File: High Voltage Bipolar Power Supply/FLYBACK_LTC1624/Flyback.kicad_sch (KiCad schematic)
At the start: 46 parts, among them J1 1715721, J2 Conn_01x02, Q1 PZT2222A, Q2 IRL540NS, T1 VP3-0138, U1 LTC1624CS8, U2 TSR_1-2450, U3 ADUM4195-1, U4 TBA1-0511E

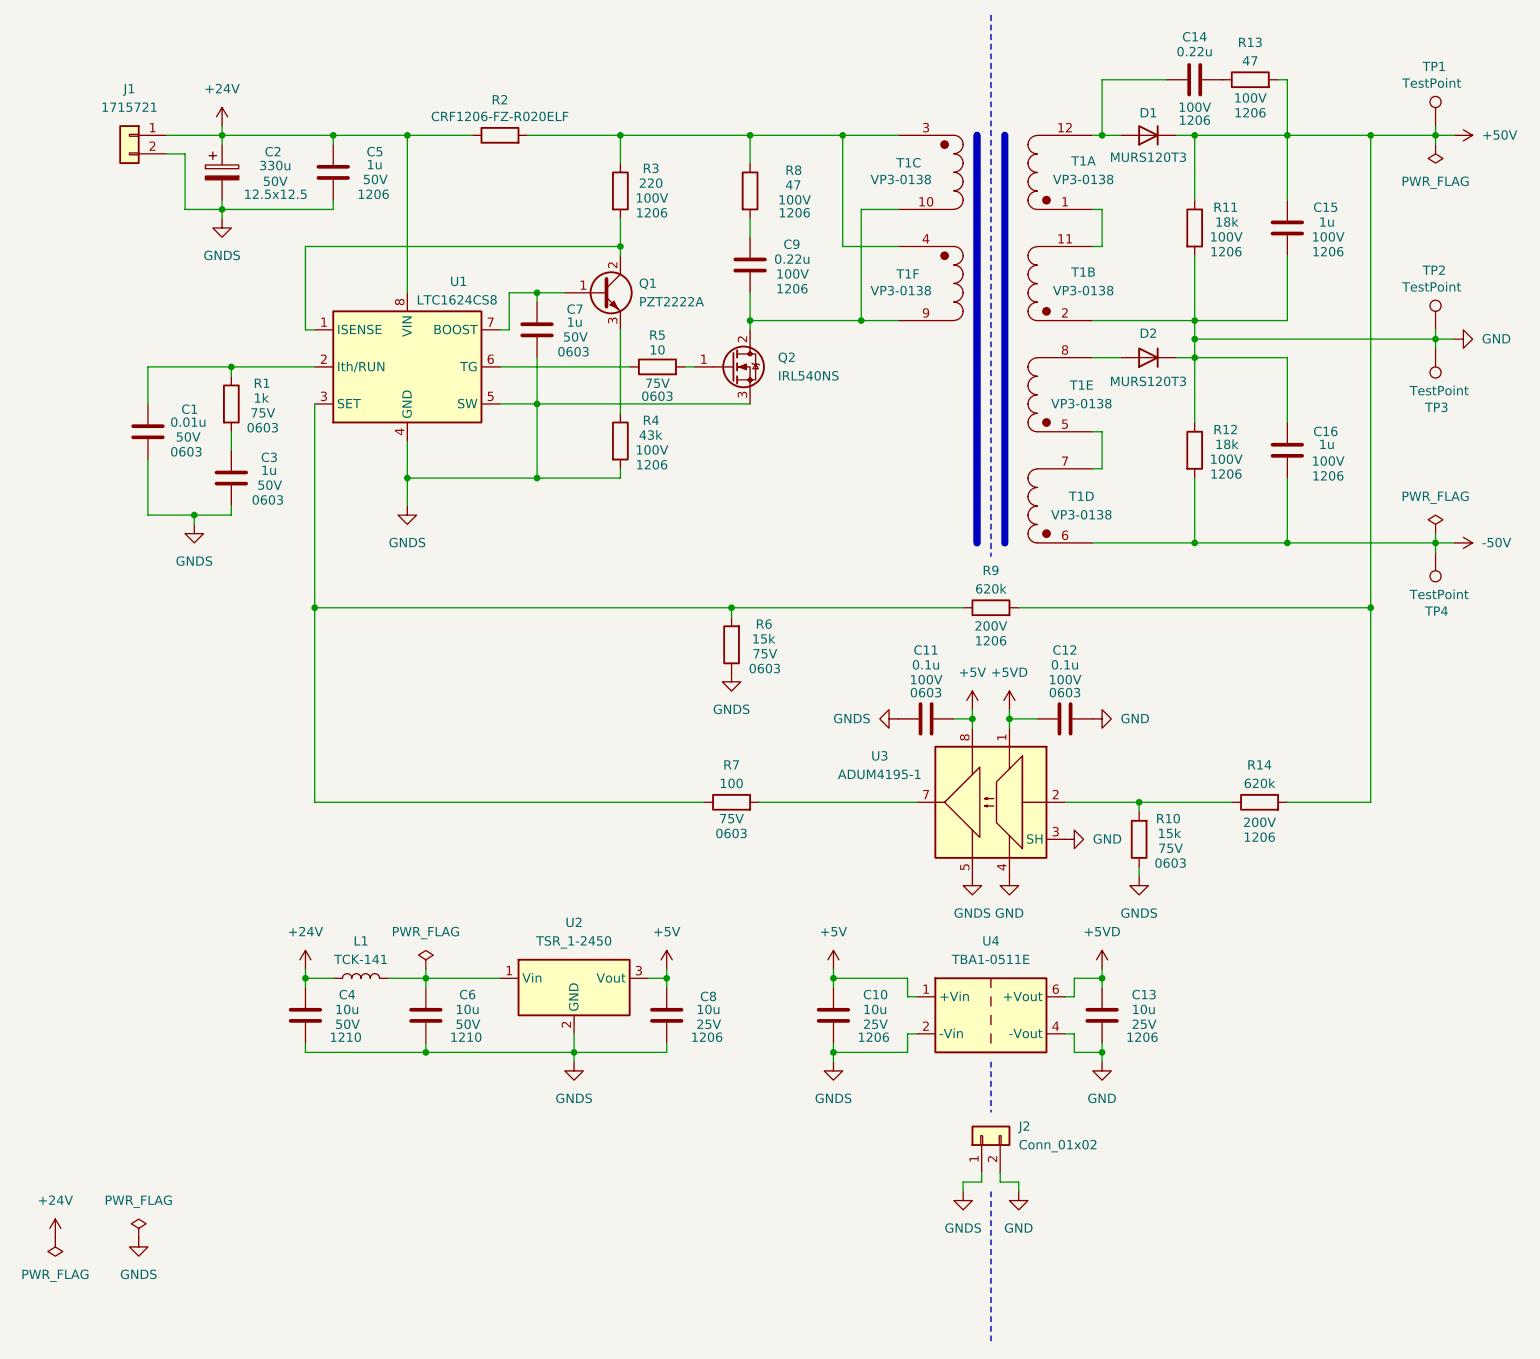
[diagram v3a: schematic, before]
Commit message: FLYBACK_LTC1624 : Design failed, can't buy LM377HV for -50V
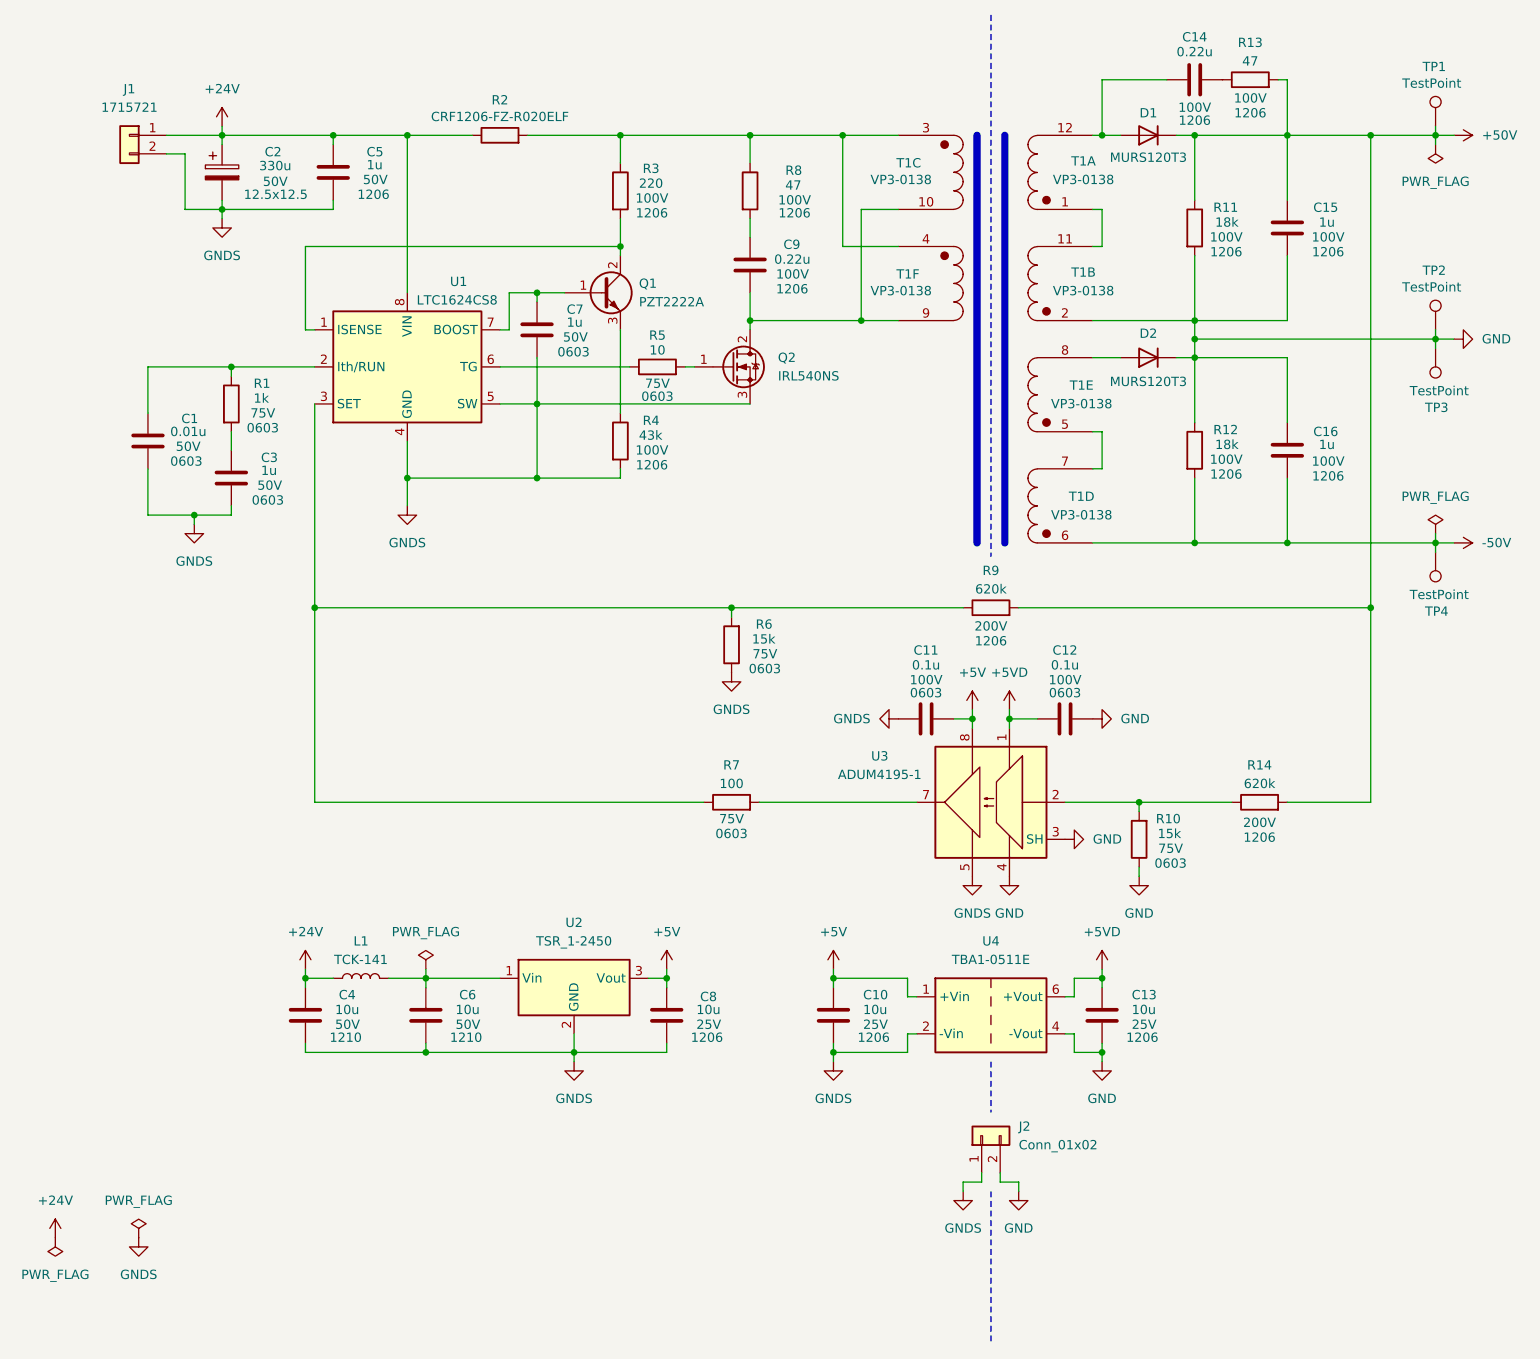
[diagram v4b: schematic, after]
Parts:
- TP1, TP2, TP3, TP4: now left out of the parts list
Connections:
- net GND: now also R10.1
- net GNDS: no longer R10.1
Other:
- moved on the sheet: C1
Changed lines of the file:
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@@
 	(wire
 		(pts
-			(xy 44.45 67.31) (xy 44.45 62.23)
+			(xy 44.45 68.58) (xy 44.45 62.23)
 		)
 		(stroke
@@
 	(wire
 		(pts
-			(xy 44.45 74.93) (xy 44.45 82.55)
+			(xy 44.45 76.2) (xy 44.45 82.55)
 		)
 		(stroke
@@
 		(unit 1)
 		(exclude_from_sim no)
-		(in_bom yes)
+		(in_bom no)
 		(on_board yes)
 		(dnp no)
@@
 		(unit 1)
 		(exclude_from_sim no)
-		(in_bom yes)
+		(in_bom no)
 		(on_board yes)
 		(dnp no)
@@
 	(symbol
 		(lib_id "power:GND")
+		(at 180.34 132.08 0)
+		(unit 1)
+		(exclude_from_sim no)
+		(in_bom yes)
+		(on_board yes)
+		(dnp no)
+		(fields_autoplaced yes)
+		(property "Reference" "#PWR024"
+			(at 180.34 138.43 0)
+			(effects
+				(font
+					(size 1.27 1.27)
+				)
+				(hide yes)
+			)
+		)
+		(property "Value" "GND"
+			(at 180.34 137.16 0)
+			(effects
+				(font
+					(size 1.27 1.27)
+				)
+			)
+		)
+		(property "Footprint" ""
+			(at 180.34 132.08 0)
+			(effects
+				(font
+					(size 1.27 1.27)
+				)
+				(hide yes)
+			)
+		)
+		(property "Datasheet" ""
+			(at 180.34 132.08 0)
+			(effects
+				(font
+					(size 1.27 1.27)
+				)
+				(hide yes)
+			)
+		)
+		(property "Description" "Power symbol creates a global label with name \"GND\" , ground"
+			(at 180.34 132.08 0)
+			(effects
+				(font
+					(size 1.27 1.27)
+				)
+				(hide yes)
+			)
+		)
+		(pin "1"
+		)
+		(instances
+			(project "FLYBACK_LTC1624"
+				(path "/b6dc4b50-1aef-431e-aae5-8ba2077040d1/0d0ff0c8-e715-47fe-aebe-0044b1d841d2"
+					(reference "#PWR024")
+					(unit 1)
+				)
+			)
+		)
+	)
+	(symbol
+		(lib_id "power:GND")
 		(at 162.56 132.08 0)
 		(unit 1)
@@
 	(symbol
 		(lib_id "Device:C")
-		(at 44.45 71.12 0)
+		(at 44.45 72.39 0)
 		(unit 1)
 		(exclude_from_sim no)
@@
 		(dnp no)
 		(property "Reference" "C1"
-			(at 49.022 68.072 0)
+			(at 49.022 69.342 0)
 			(effects
 				(font
@@
 		)
 		(property "Value" "0.01u"
-			(at 47.498 69.85 0)
+			(at 47.498 71.12 0)
 			(effects
 				(font
@@
 		)
 		(property "Footprint" "Capacitor_SMD:C_0603_1608Metric_Pad1.08x0.95mm_HandSolder"
-			(at 45.4152 74.93 0)
+			(at 45.4152 76.2 0)
 			(effects
 				(font
@@
 		)
 		(property "Datasheet" "~"
-			(at 44.45 71.12 0)
+			(at 44.45 72.39 0)
 			(effects
 				(font
@@
 		)
 		(property "Description" "Unpolarized capacitor"
-			(at 44.45 71.12 0)
+			(at 44.45 72.39 0)
 			(effects
 				(font
@@
 		)
 		(property "Voltage" "50V"
-			(at 48.26 71.882 0)
+			(at 48.26 73.152 0)
 			(effects
 				(font
@@
 		)
 		(property "Package" "0603"
-			(at 47.498 73.914 0)
+			(at 47.498 75.184 0)
 			(effects
 				(font
@@
 	)
 	(symbol
-		(lib_id "power:GNDS")
-		(at 180.34 132.08 0)
-		(unit 1)
-		(exclude_from_sim no)
-		(in_bom yes)
-		(on_board yes)
-		(dnp no)
-		(fields_autoplaced yes)
-		(property "Reference" "#PWR024"
-			(at 180.34 138.43 0)
-			(effects
-				(font
-					(size 1.27 1.27)
-				)
-				(hide yes)
-			)
-		)
-		(property "Value" "GNDS"
-			(at 180.34 137.16 0)
-			(effects
-				(font
-					(size 1.27 1.27)
-				)
-			)
-		)
-		(property "Footprint" ""
-			(at 180.34 132.08 0)
-			(effects
-				(font
-					(size 1.27 1.27)
-				)
-				(hide yes)
-			)
-		)
-		(property "Datasheet" ""
-			(at 180.34 132.08 0)
-			(effects
-				(font
-					(size 1.27 1.27)
-				)
-				(hide yes)
-			)
-		)
-		(property "Description" "Power symbol creates a global label with name \"GNDS\" , signal ground"
-			(at 180.34 132.08 0)
-			(effects
-				(font
-					(size 1.27 1.27)
-				)
-				(hide yes)
-			)
-		)
-		(pin "1"
-		)
-		(instances
-			(project "FLYBACK_LTC1624"
-				(path "/b6dc4b50-1aef-431e-aae5-8ba2077040d1/0d0ff0c8-e715-47fe-aebe-0044b1d841d2"
-					(reference "#PWR024")
-					(unit 1)
-				)
-			)
-		)
-	)
-	(symbol
 		(lib_id "Device:C")
 		(at 138.43 151.13 0)
@@
 		(unit 1)
 		(exclude_from_sim no)
-		(in_bom yes)
+		(in_bom no)
 		(on_board yes)
 		(dnp no)
@@
 		(unit 1)
 		(exclude_from_sim no)
-		(in_bom yes)
+		(in_bom no)
 		(on_board yes)
 		(dnp no)
